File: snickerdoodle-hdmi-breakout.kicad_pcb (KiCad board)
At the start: 4 copper layers, 62.2 x 19.7 mm, 45 parts, among them J1 SMH-120-02-T-D, J2 685119134923, J3 solder_jumper, Q1 BSS138AKA, Q2 BSS138AKA, Q3 BSS138AKA, U1 TPD12S016PWR, U2 TPS61232DRCT

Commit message: Updated component library
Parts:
- 3V3, 5V0, LED1, LED2: footprint krtkl-breakybreaky-hdmi-expansion-footprints:LED_0603 -> snickerdoodle-hdmi-breakout-footprints:LED_0603
- C1, C2, C3, C5: footprint krtkl-breakybreaky-hdmi-expansion-footprints:0402-cap -> snickerdoodle-hdmi-breakout-footprints:0402-cap
- C4, C6, C7, C8: footprint krtkl-breakybreaky-hdmi-expansion-footprints:0805-cap -> snickerdoodle-hdmi-breakout-footprints:0805-cap
- D1: footprint krtkl-breakybreaky-hdmi-expansion-footprints:SOD-323F -> snickerdoodle-hdmi-breakout-footprints:SOD-323F
- FB1, R12, R9: footprint krtkl-breakybreaky-hdmi-expansion-footprints:0603-res -> snickerdoodle-hdmi-breakout-footprints:0603-res
- J1: footprint krtkl-breakybreaky-hdmi-expansion-footprints:SMH-120-02-T-D -> snickerdoodle-hdmi-breakout-footprints:SMH-120-02-T-D
- J2: footprint krtkl-breakybreaky-hdmi-expansion-footprints:HDMI_A_Female_685119134923 -> snickerdoodle-hdmi-breakout-footprints:HDMI_A_Female_685119134923
- J3: footprint krtkl-breakybreaky-hdmi-expansion-footprints:SolderJumper-0.6x1.4mm -> snickerdoodle-hdmi-breakout-footprints:SolderJumper-0.6x1.4mm
- L1: footprint krtkl-breakybreaky-hdmi-expansion-footprints:XFL4020-102MEB -> snickerdoodle-hdmi-breakout-footprints:XFL4020-102MEB
- N1: footprint krtkl-breakybreaky-hdmi-expansion-footprints:oshw-logo -> snickerdoodle-hdmi-breakout-footprints:oshw-logo
- N2: footprint krtkl-breakybreaky-hdmi-expansion-footprints:antmicro-logo_scaled_20mm -> snickerdoodle-hdmi-breakout-footprints:antmicro-logo_scaled_20mm
- Q1, Q2, Q3: footprint krtkl-breakybreaky-hdmi-expansion-footprints:SOT-23-3 -> snickerdoodle-hdmi-breakout-footprints:SOT-23-3
- R1, R10, R11, R13, R14, R2, R3, R4, R5, R6, R7, R8: footprint krtkl-breakybreaky-hdmi-expansion-footprints:0402-res -> snickerdoodle-hdmi-breakout-footprints:0402-res
- TP1, TP2, TP3, TP4, TP5, TP6: footprint krtkl-breakybreaky-hdmi-expansion-footprints:Testpoint_smd_1mm -> snickerdoodle-hdmi-breakout-footprints:Testpoint_smd_1mm
- U1: footprint krtkl-breakybreaky-hdmi-expansion-footprints:TPD12S016PWR -> snickerdoodle-hdmi-breakout-footprints:TPD12S016PWR
- U2: footprint krtkl-breakybreaky-hdmi-expansion-footprints:VSON-10-1EP_3x3mm -> snickerdoodle-hdmi-breakout-footprints:VSON-10-1EP_3x3mm

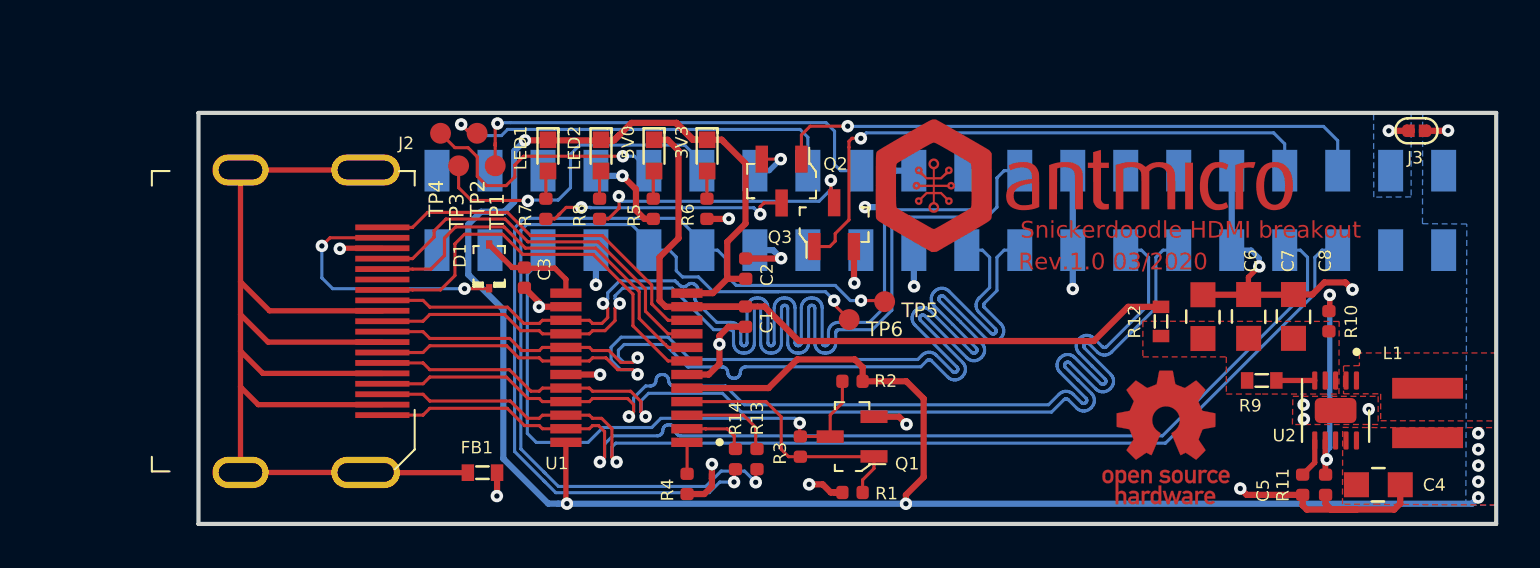
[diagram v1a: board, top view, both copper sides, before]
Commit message: Prepared files for revision 1.1.0 - rotated HDMI connector, changed PCB size
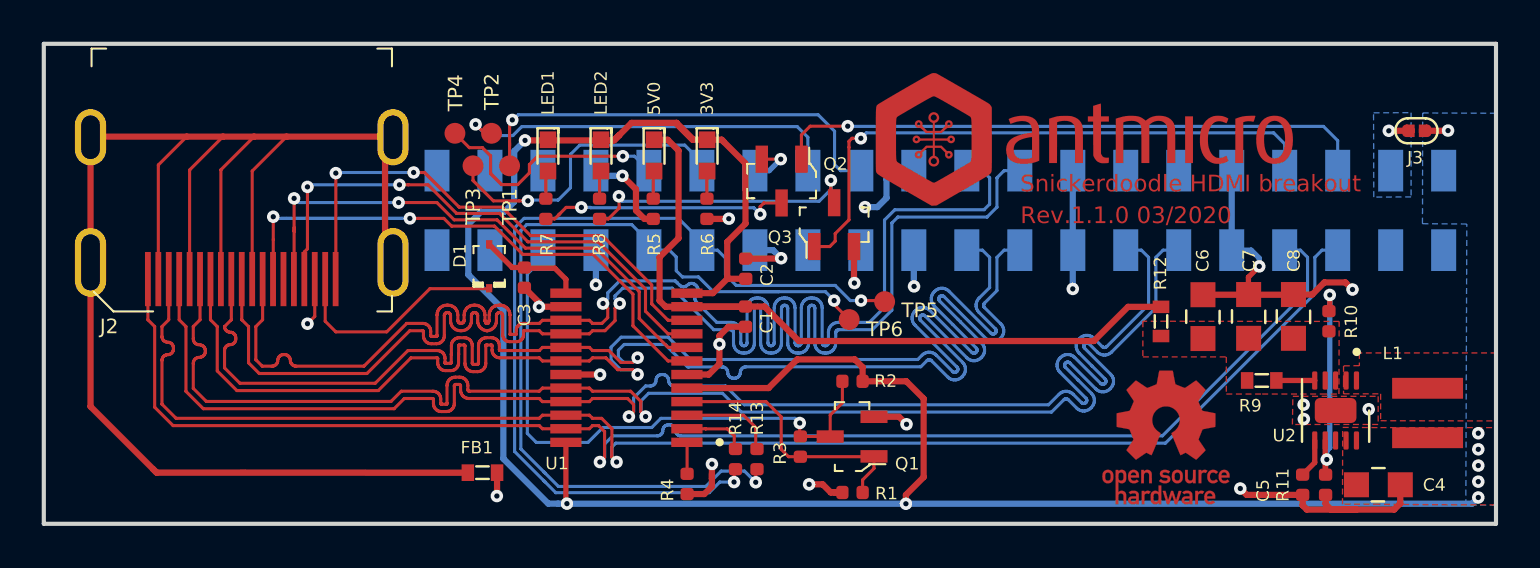
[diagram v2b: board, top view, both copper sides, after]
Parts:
- J2: footprint snickerdoodle-hdmi-breakout-footprints:HDMI_A_Female_685119134923 -> antmicro-footprints:HDMI_A_Female_685119134923
- moved J2 6.37 mm to (132.2, 109.2), turned to 0 degrees
- moved N2 2.22 mm to (172.6, 104.0)
- moved TP1 0.69 mm to (145.1, 105.1)
- moved TP2 0.69 mm to (144.2, 103.5)
- moved TP3 0.69 mm to (143.3, 105.1)
- moved TP4 0.69 mm to (142.5, 103.5)
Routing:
- net Earth: track 60.5 -> 99.5 mm
- net /TMDS_DATA0_N: track 53.9 -> 71.2 mm
- net /TMDS_DATA0_P: track 53.9 -> 71.1 mm
- net /TMDS_CLK_N: track 54.0 -> 71.2 mm
- net /TMDS_DATA2_N: track 54.0 -> 71.2 mm
- net /TMDS_DATA2_P: track 54.1 -> 71.1 mm
- net /TMDS_DATA1_N: track 54.1 -> 71.1 mm
- net /TMDS_CLK_P: track 54.0 -> 70.9 mm
- net /TMDS_DATA1_P: track 54.1 -> 71.1 mm
- net /HDMI_CEC_5V: track 20.0 -> 33.8 mm, vias 0 -> 2
- net /HDMI_SDA_5V: track 18.5 -> 27.5 mm, vias 0 -> 2
- net /HDMI_HPD_5V: track 17.6 -> 26.5 mm, vias 0 -> 2
- net /HDMI_SCL_5V: track 19.1 -> 27.6 mm, vias 0 -> 2
- net Net-(D1-PadK): track 12.8 -> 11.0 mm, vias 2 -> 0
- net /IO_L16N_T2_34: track 12.8 -> 11.9 mm
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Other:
- board size 62.2 x 19.7 mm -> 69.6 x 23 mm
- board text added: "Rev.1.1.0 03/2020"
- board text removed: "Rev.1.0 03/2020"

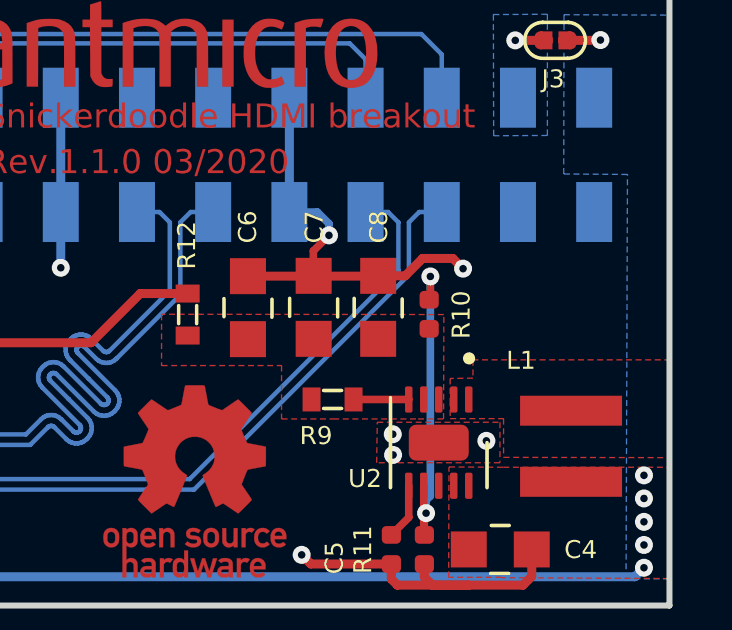
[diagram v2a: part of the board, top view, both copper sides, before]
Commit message: Changed R10, re-generated documentation
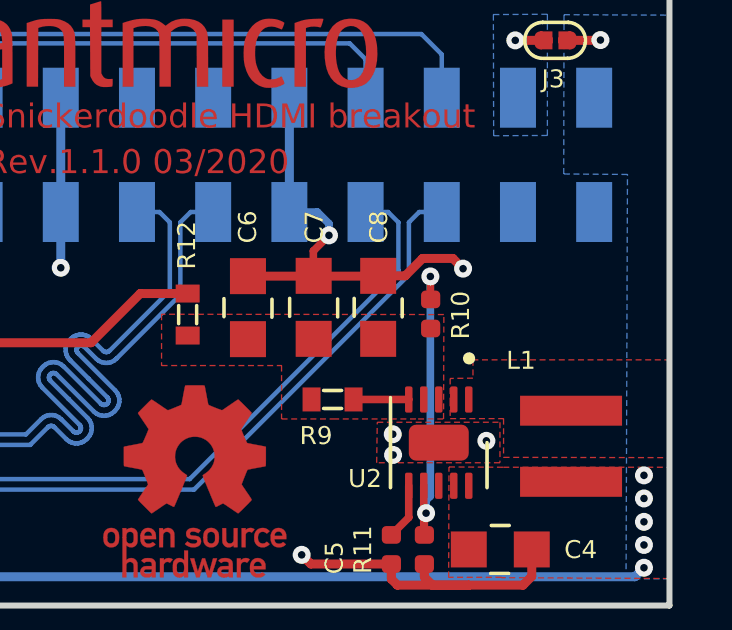
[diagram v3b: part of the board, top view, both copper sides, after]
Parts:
- J2: footprint antmicro-footprints:HDMI_A_Female_685119134923 -> snickerdoodle-hdmi-breakout-footprints:HDMI_A_Female_685119134923
- R10: value R_402k_0402 -> R_0R_0402
- moved R10 0.05 mm to (184.4, 112.5)
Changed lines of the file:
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@@
-(kicad_pcb (version 20171130) (host pcbnew 5.0.2+dfsg1-1)
+(kicad_pcb (version 20171130) (host pcbnew 5.1.5+dfsg1-2~bpo10+1)
   (general
     (thickness 1.6)
@@
     (zone_45_only no)
     (trace_min 0.15)
-    (segment_width 0.2)
-    (edge_width 0.05)
     (via_size 0.6)
     (via_drill 0.25)
@@
     (uvia_min_size 0.2)
     (uvia_min_drill 0.1)
+    (edge_width 0.05)
+    (segment_width 0.2)
     (pcb_text_width 0.3)
     (pcb_text_size 1.5 1.5)
@@
       (drillshape 0)
       (scaleselection 1)
-      (outputdirectory "./gerber/"))
+      (outputdirectory "./pcb"))
   )
   (net 0 "")
@@
     (uvia_dia 0.3)
     (uvia_drill 0.1)
+    (diff_pair_width 0.15)
     (diff_pair_gap 0.2)
-    (diff_pair_width 0.15)
     (add_net /GP_LED1)
     (add_net /GP_LED2)
@@
     (add_net "Net-(U2-Pad8)")
   )
-  (module antmicro-footprints:HDMI_A_Female_685119134923 (layer F.Cu)
+  (module snickerdoodle-hdmi-breakout-footprints:0402-res (layer F.Cu)
+    (at 184.41 112.48 90)
+    (descr "Resistor SMD 0402 (1005 Metric), square (rectangular) end terminal, IPC_7351 nominal, (Body size source: http://www.tortai-tech.com/upload/download/2011102023233369053.pdf), generated with kicad-footprint-generator")
+    (tags resistor)
+    (attr smd)
+    (fp_text reference R10 (at -0.04 1 90) (layer F.SilkS)
+      (effects (font (size 0.6 0.6) (thickness 0.15)))
+    )
+    (fp_text value R_0R_0402 (at 0 1.17 90) (layer F.Fab)
+      (effects (font (size 1 1) (thickness 0.15)))
+    )
+    (fp_text user %R (at 0 0 90) (layer F.Fab)
+      (effects (font (size 0.25 0.25) (thickness 0.04)))
+    )
+    (fp_line (start 0.93 0.47) (end -0.93 0.47) (layer F.CrtYd) (width 0.05))
+    (fp_line (start 0.93 -0.47) (end 0.93 0.47) (layer F.CrtYd) (width 0.05))
+    (fp_line (start -0.93 -0.47) (end 0.93 -0.47) (layer F.CrtYd) (width 0.05))
+    (fp_line (start -0.93 0.47) (end -0.93 -0.47) (layer F.CrtYd) (width 0.05))
+    (fp_line (start 0.5 0.25) (end -0.5 0.25) (layer F.Fab) (width 0.1))
+    (fp_line (start 0.5 -0.25) (end 0.5 0.25) (layer F.Fab) (width 0.1))
+    (fp_line (start -0.5 -0.25) (end 0.5 -0.25) (layer F.Fab) (width 0.1))
+    (fp_line (start -0.5 0.25) (end -0.5 -0.25) (layer F.Fab) (width 0.1))
+    (pad 2 smd roundrect (at 0.485 0 90) (size 0.59 0.64) (layers F.Cu F.Paste F.Mask) (roundrect_rratio 0.25)
+      (net 45 "Net-(R10-Pad2)"))
+    (pad 1 smd roundrect (at -0.485 0 90) (size 0.59 0.64) (layers F.Cu F.Paste F.Mask) (roundrect_rratio 0.25)
+      (net 51 "Net-(C6-Pad1)"))
+    (model ${KIPRJMOD}/lib/3d-models/0402-res.step
+      (offset (xyz 0 0 -0.01))
+      (scale (xyz 1 1 1))
+      (rotate (xyz 0 0 0))
+    )
+  )
+  (module snickerdoodle-hdmi-breakout-footprints:HDMI_A_Female_685119134923 (layer F.Cu)
     (at 132.24 109.17)
     (descr http://media.digikey.com/pdf/Data%20Sheets/CNC%20Tech%20PDFs/HDMI_A_Female_2000-1-2-41-00-BK_Dwg.pdf)
@@
     (pad SH thru_hole oval (at -7.25 -5.5) (size 1.5 2.7) (drill oval 0.9 2.1) (layers *.Cu *.Mask)
       (net 54 Earth))
-    (model ${ANT3DMDL}/685119134923.stp
+    (model ${KIPRJMOD}/lib/3d-models/685119134923.stp
       (offset (xyz 0 1 4.1))
       (scale (xyz 1 1 1))
@@
     (model ${KIPRJMOD}/lib/3d-models/0402-res.step
       (offset (xyz 0 0 -0.01))
-      (scale (xyz 1 1 1))
-      (rotate (xyz 0 0 0))
-    )
-  )
-  (module snickerdoodle-hdmi-breakout-footprints:0402-res (layer F.Cu)
-    (at 184.36 112.49 90)
-    (descr "Resistor SMD 0402 (1005 Metric), square (rectangular) end terminal, IPC_7351 nominal, (Body size source: http://www.tortai-tech.com/upload/download/2011102023233369053.pdf), generated with kicad-footprint-generator")
-    (tags resistor)
-    (attr smd)
-    (fp_text reference R10 (at -0.02 1.07 90) (layer F.SilkS)
-      (effects (font (size 0.6 0.6) (thickness 0.15)))
-    )
-    (fp_text value R_402k_0402 (at 0 1.17 90) (layer F.Fab)
-      (effects (font (size 0.6 0.6) (thickness 0.15)))
-    )
-    (fp_text user %R (at 0 0 90) (layer F.Fab)
-      (effects (font (size 0.6 0.6) (thickness 0.15)))
-    )
-    (fp_line (start 0.93 0.47) (end -0.93 0.47) (layer F.CrtYd) (width 0.05))
-    (fp_line (start 0.93 -0.47) (end 0.93 0.47) (layer F.CrtYd) (width 0.05))
-    (fp_line (start -0.93 -0.47) (end 0.93 -0.47) (layer F.CrtYd) (width 0.05))
-    (fp_line (start -0.93 0.47) (end -0.93 -0.47) (layer F.CrtYd) (width 0.05))
-    (fp_line (start 0.5 0.25) (end -0.5 0.25) (layer F.Fab) (width 0.1))
-    (fp_line (start 0.5 -0.25) (end 0.5 0.25) (layer F.Fab) (width 0.1))
-    (fp_line (start -0.5 -0.25) (end 0.5 -0.25) (layer F.Fab) (width 0.1))
-    (fp_line (start -0.5 0.25) (end -0.5 -0.25) (layer F.Fab) (width 0.1))
-    (pad 2 smd roundrect (at 0.485 0 90) (size 0.59 0.64) (layers F.Cu F.Paste F.Mask) (roundrect_rratio 0.25)
-      (net 45 "Net-(R10-Pad2)"))
-    (pad 1 smd roundrect (at -0.485 0 90) (size 0.59 0.64) (layers F.Cu F.Paste F.Mask) (roundrect_rratio 0.25)
-      (net 51 "Net-(C6-Pad1)"))
-    (model ${KIPRJMOD}/lib/3d-models/0402-res.step
-      (offset (xyz 0 0 -0.01))
